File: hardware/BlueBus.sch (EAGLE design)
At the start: 128 parts, among them Q1 NMOSFET-BSS138K, Q2 PMOSFET-DMP1045UQ, Q3 NMOSFET-BSS138K, X1 CRYSTAL-12MHZ

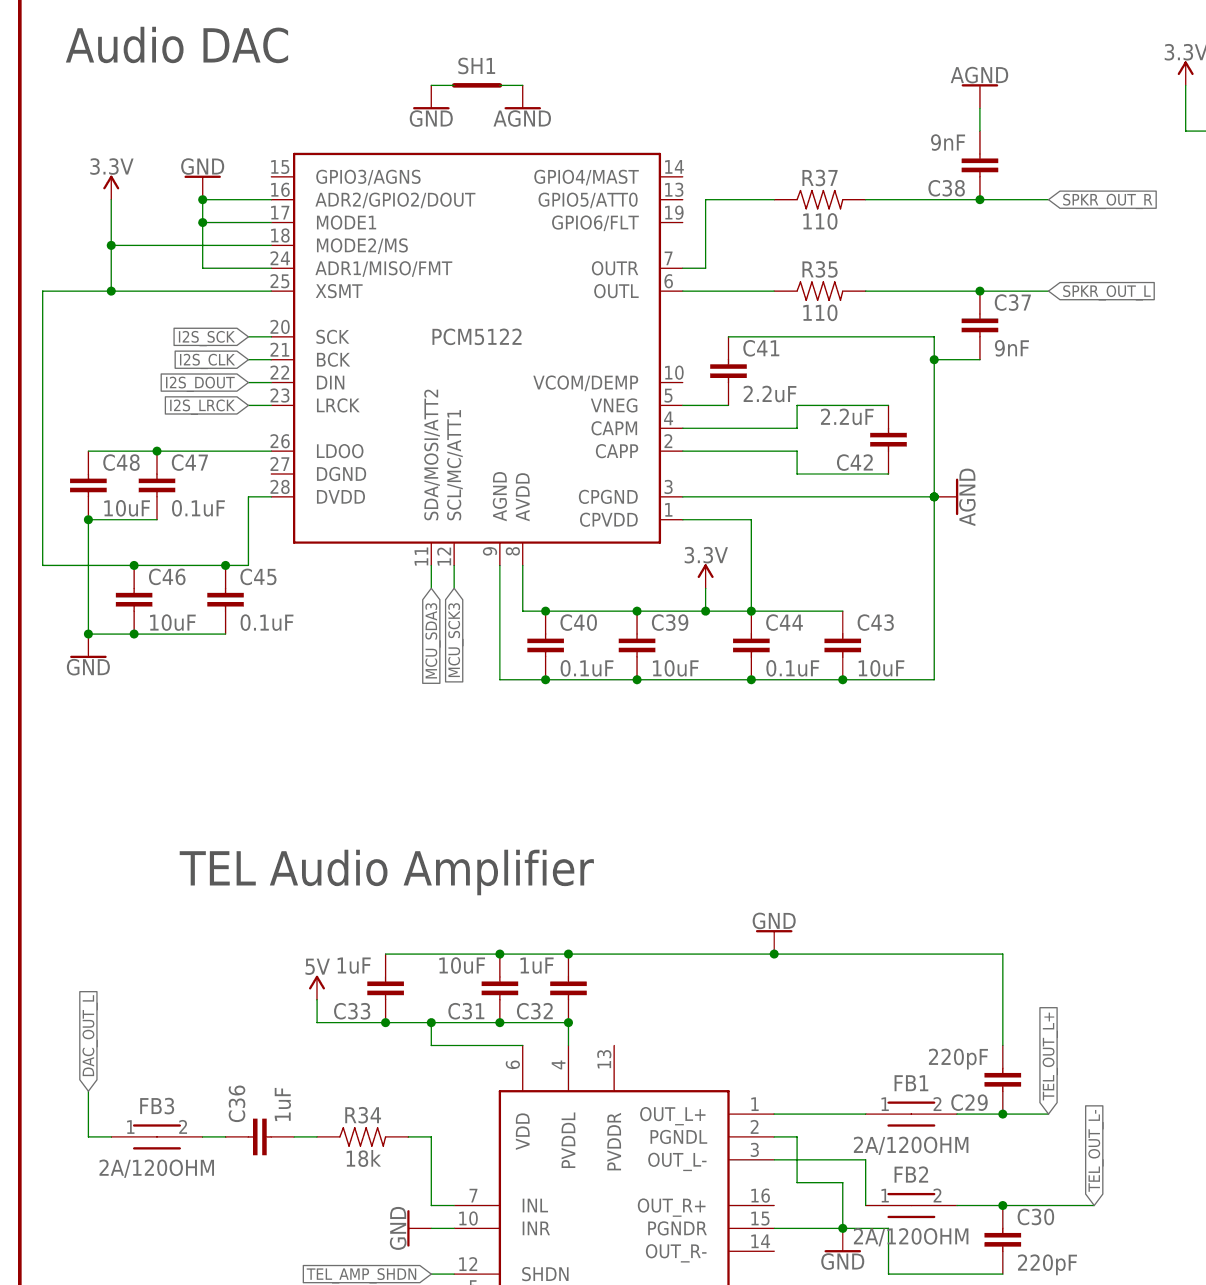
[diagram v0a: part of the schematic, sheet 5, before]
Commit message: [IMP] hardware: Revision D.1 * Remove errant layers
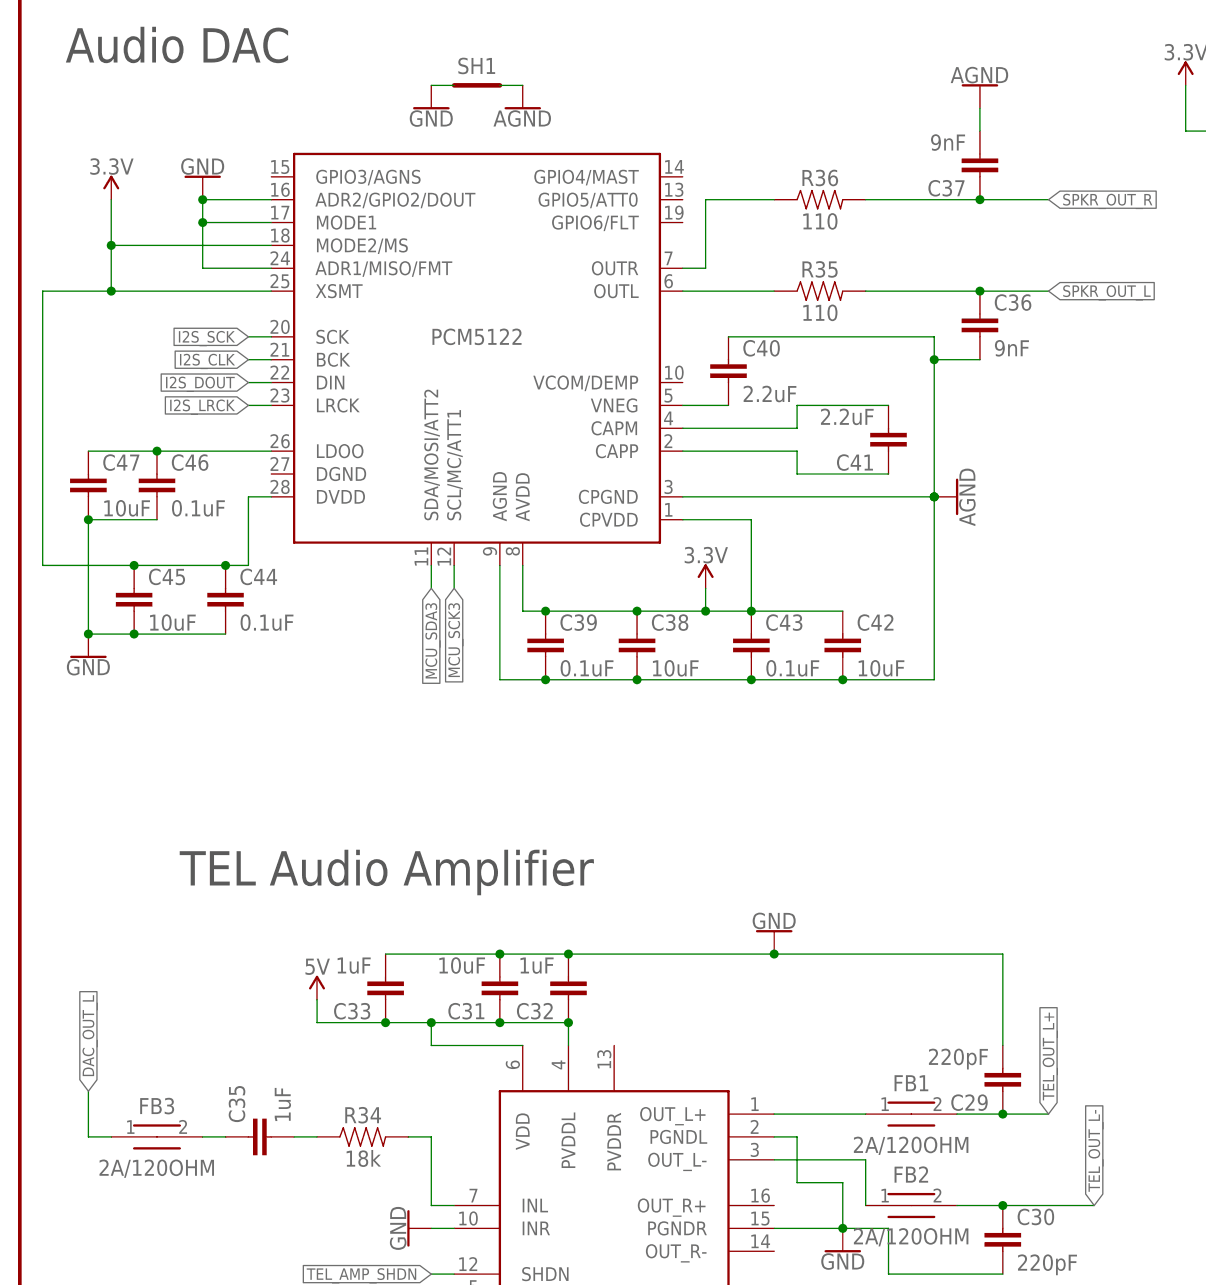
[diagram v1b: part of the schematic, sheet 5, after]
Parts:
- removed C48: 10uF, Passives:10UF2012
- added C35: 1uF, Passives:1UF
- C36: value 1uF -> 9nF; device Passives:1UF -> Passives:9NF
- C38: value 9nF -> 10uF; device Passives:9NF -> Passives:10UF2012
- C39, C43, C46: value 10uF -> 0.1uF; device Passives:10UF2012 -> Passives:0.1UF
- C40: value 0.1uF -> 2.2uF; device Passives:0.1UF -> Passives:2.2UF
- C42: value 2.2uF -> 10uF; device Passives:2.2UF -> Passives:10UF2012
- C45, C47: value 0.1uF -> 10uF; device Passives:0.1UF -> Passives:10UF2012
- renumbered R37 to R36
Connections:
- net 3.3V: now also C38.1, C42.1; no longer C40.1, C46.1
- net AGND: now also C36.2, C40.1, C42.2; no longer C40.2, C41.1, C44.2
- net DAC_CAPM: now also C41.2; no longer C42.2
- net DAC_CAPP: now also C41.1; no longer C42.1
- net DAC_LDOO: now also C46.1; no longer C48.1
- net DAC_VNEG: now also C40.2; no longer C41.2
- net GND: now also C44.2; no longer C48.2
- net SPKR_OUT_L: now also C36.1; no longer C37.1
- net SPKR_OUT_R: now also C37.1; no longer C38.1
- net TEL_AMP_IN: now also C35.1; no longer C36.1
- net TEL_AMP_INL_CAP_RES: now also C35.2; no longer C36.2
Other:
- moved on the sheet: C36, C37, C38, C39, C40, C41, C42, C43, C44, C45, C46, C47

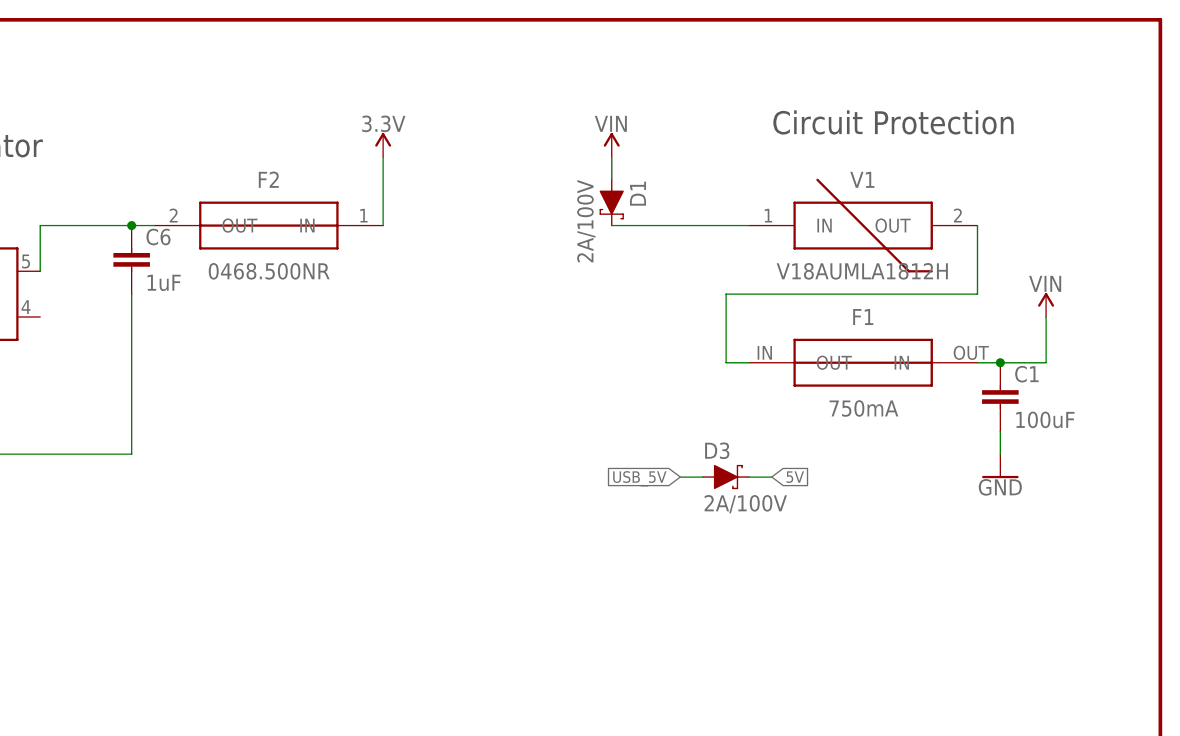
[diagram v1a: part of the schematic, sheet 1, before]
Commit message: [IMP] hardware: Update Varistor wiring * Improve Schematic drawing for circuit protection
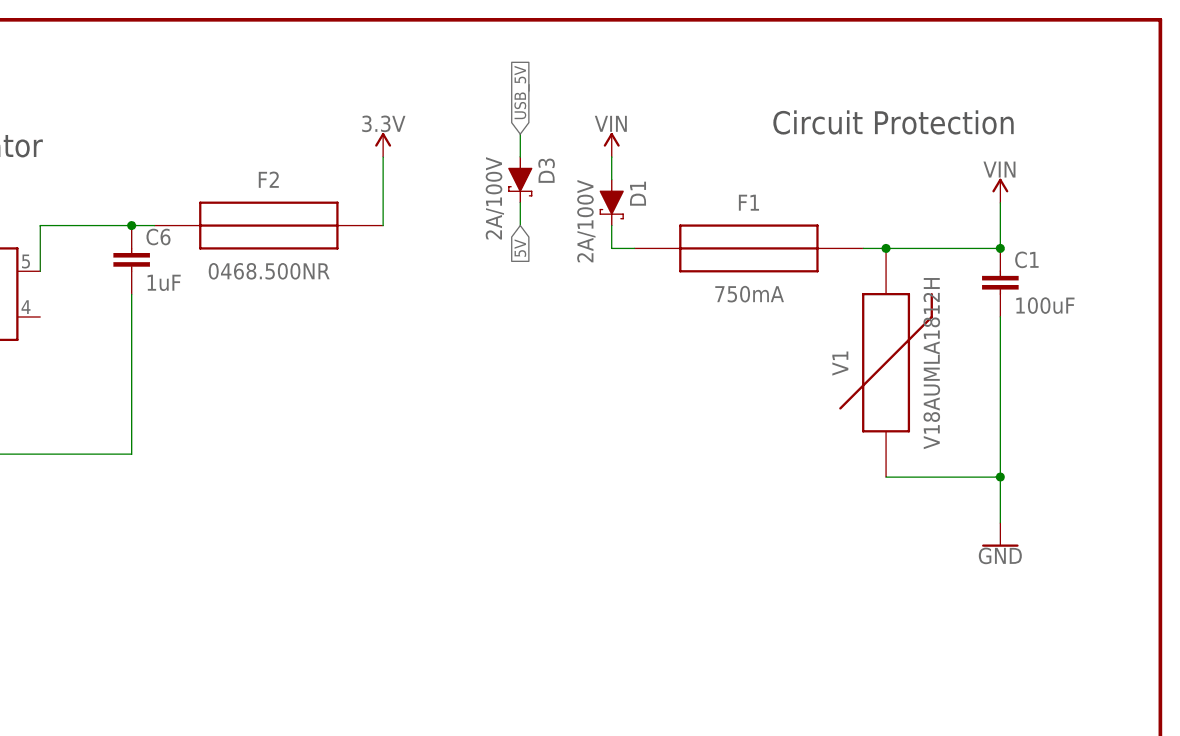
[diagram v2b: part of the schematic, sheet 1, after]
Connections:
- net GND: now also V1.IN
- net VIN: no longer V1.IN
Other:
- moved on the sheet: C1, D3
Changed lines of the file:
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@@
 <layers>
 <layer number="1" name="Top" color="4" fill="1" visible="no" active="no"/>
+<layer number="2" name="Route2" color="1" fill="3" visible="no" active="no"/>
+<layer number="3" name="Route3" color="4" fill="3" visible="no" active="no"/>
+<layer number="4" name="Route4" color="1" fill="4" visible="no" active="no"/>
+<layer number="5" name="Route5" color="4" fill="4" visible="no" active="no"/>
+<layer number="6" name="Route6" color="1" fill="8" visible="no" active="no"/>
+<layer number="7" name="Route7" color="4" fill="8" visible="no" active="no"/>
+<layer number="8" name="Route8" color="1" fill="2" visible="no" active="no"/>
+<layer number="9" name="Route9" color="4" fill="2" visible="no" active="no"/>
+<layer number="10" name="Route10" color="1" fill="7" visible="no" active="no"/>
+<layer number="11" name="Route11" color="4" fill="7" visible="no" active="no"/>
+<layer number="12" name="Route12" color="1" fill="5" visible="no" active="no"/>
+<layer number="13" name="Route13" color="4" fill="5" visible="no" active="no"/>
+<layer number="14" name="Route14" color="1" fill="6" visible="no" active="no"/>
+<layer number="15" name="Route15" color="4" fill="6" visible="no" active="no"/>
 <layer number="16" name="Bottom" color="1" fill="1" visible="no" active="no"/>
 <layer number="17" name="Pads" color="2" fill="1" visible="no" active="no"/>
@@
 <attribute name="NAME" x="71.628" y="101.6" size="1.778" layer="95" font="vector" rot="R270"/>
 </instance>
-<instance part="D3" gate="G$1" x="200.66" y="134.62" smashed="yes">
-<attribute name="NAME" x="198.12" y="136.652" size="1.778" layer="95" font="vector"/>
-<attribute name="VALUE" x="198.12" y="132.588" size="1.778" layer="96" font="vector" align="top-left"/>
-</instance>
-<instance part="C1" gate="G$1" x="231.14" y="142.24" smashed="yes">
-<attribute name="NAME" x="232.664" y="145.161" size="1.778" layer="95" font="vector"/>
-<attribute name="VALUE" x="232.664" y="140.081" size="1.778" layer="96" font="vector"/>
+<instance part="D3" gate="G$1" x="177.8" y="167.64" smashed="yes" rot="R270">
+<attribute name="NAME" x="179.832" y="170.18" size="1.778" layer="95" font="vector" rot="R270"/>
+<attribute name="VALUE" x="175.768" y="170.18" size="1.778" layer="96" font="vector" rot="R270" align="top-left"/>
+</instance>
+<instance part="C1" gate="G$1" x="231.14" y="154.94" smashed="yes">
+<attribute name="NAME" x="232.664" y="157.861" size="1.778" layer="95" font="vector"/>
+<attribute name="VALUE" x="232.664" y="152.781" size="1.778" layer="96" font="vector"/>
 </instance>
 <instance part="SPKR_OUT" gate="G$1" x="66.04" y="53.34" smashed="yes">
@@
 <attribute name="NAME" x="46.228" y="101.6" size="1.778" layer="95" font="vector" rot="R270"/>
 </instance>
-<instance part="GND17" gate="1" x="231.14" y="134.62" smashed="yes">
-<attribute name="VALUE" x="231.14" y="134.366" size="1.778" layer="96" align="top-center"/>
+<instance part="GND17" gate="1" x="231.14" y="127" smashed="yes">
+<attribute name="VALUE" x="231.14" y="126.746" size="1.778" layer="96" align="top-center"/>
 </instance>
 <instance part="XRP7659" gate="G$1" x="30.48" y="154.94" smashed="yes">
@@
 <attribute name="VALUE" x="25.4" y="14.986" size="1.778" layer="96" align="top-center"/>
 </instance>
-<instance part="V1" gate="G$1" x="215.9" y="162.56" smashed="yes">
-<attribute name="NAME" x="215.9" y="167.64" size="1.778" layer="95" font="vector" rot="MR0" align="center"/>
-<attribute name="VALUE" x="215.9" y="157.48" size="1.778" layer="96" font="vector" rot="MR0" align="center"/>
-</instance>
-<instance part="SUPPLY12" gate="G$1" x="236.22" y="152.4" smashed="yes">
-<attribute name="VALUE" x="236.22" y="155.194" size="1.778" layer="96" align="bottom-center"/>
-</instance>
-<instance part="F1" gate="G$1" x="215.9" y="147.32" smashed="yes">
-<attribute name="NAME" x="215.9" y="152.4" size="1.778" layer="95" font="vector" align="center"/>
-<attribute name="VALUE" x="215.9" y="142.24" size="1.778" layer="96" font="vector" align="center"/>
+<instance part="V1" gate="G$1" x="218.44" y="147.32" smashed="yes" rot="R90">
+<attribute name="NAME" x="213.36" y="147.32" size="1.778" layer="95" font="vector" rot="MR270" align="center"/>
+<attribute name="VALUE" x="223.52" y="147.32" size="1.778" layer="96" font="vector" rot="MR270" align="center"/>
+</instance>
+<instance part="SUPPLY12" gate="G$1" x="231.14" y="165.1" smashed="yes">
+<attribute name="VALUE" x="231.14" y="167.894" size="1.778" layer="96" align="bottom-center"/>
+</instance>
+<instance part="F1" gate="G$1" x="203.2" y="160.02" smashed="yes">
+<attribute name="NAME" x="203.2" y="165.1" size="1.778" layer="95" font="vector" align="center"/>
+<attribute name="VALUE" x="203.2" y="154.94" size="1.778" layer="96" font="vector" align="center"/>
 </instance>
 <instance part="F2" gate="G$1" x="149.86" y="162.56" smashed="yes">
@@
 <pinref part="C1" gate="G$1" pin="2"/>
 <pinref part="GND17" gate="1" pin="GND"/>
-<wire x1="231.14" y1="139.7" x2="231.14" y2="137.16" width="0.1524" layer="91"/>
+<wire x1="231.14" y1="152.4" x2="231.14" y2="134.62" width="0.1524" layer="91"/>
+<pinref part="V1" gate="G$1" pin="IN"/>
+<wire x1="231.14" y1="134.62" x2="231.14" y2="129.54" width="0.1524" layer="91"/>
+<wire x1="218.44" y1="134.62" x2="231.14" y2="134.62" width="0.1524" layer="91"/>
+<junction x="231.14" y="134.62"/>
 </segment>
 </net>
@@
 <segment>
 <pinref part="C1" gate="G$1" pin="1"/>
-<wire x1="231.14" y1="147.32" x2="236.22" y2="147.32" width="0.1524" layer="91"/>
-<wire x1="236.22" y1="147.32" x2="236.22" y2="152.4" width="0.1524" layer="91"/>
+<wire x1="231.14" y1="160.02" x2="231.14" y2="165.1" width="0.1524" layer="91"/>
 <pinref part="SUPPLY12" gate="G$1" pin="VIN"/>
-<wire x1="228.6" y1="147.32" x2="231.14" y2="147.32" width="0.1524" layer="91"/>
-<junction x="231.14" y="147.32"/>
 <pinref part="F1" gate="G$1" pin="IN"/>
+<pinref part="V1" gate="G$1" pin="OUT"/>
+<wire x1="215.9" y1="160.02" x2="218.44" y2="160.02" width="0.1524" layer="91"/>
+<wire x1="218.44" y1="160.02" x2="231.14" y2="160.02" width="0.1524" layer="91"/>
+<junction x="218.44" y="160.02"/>
+<junction x="231.14" y="160.02"/>
 </segment>
 <segment>
 <pinref part="D1" gate="G$1" pin="C"/>
-<pinref part="V1" gate="G$1" pin="IN"/>
-<wire x1="187.96" y1="162.56" x2="203.2" y2="162.56" width="0.1524" layer="91"/>
-</segment>
-<segment>
-<pinref part="V1" gate="G$1" pin="OUT"/>
-<wire x1="228.6" y1="162.56" x2="228.6" y2="154.94" width="0.1524" layer="91"/>
-<wire x1="228.6" y1="154.94" x2="200.66" y2="154.94" width="0.1524" layer="91"/>
-<wire x1="200.66" y1="154.94" x2="200.66" y2="147.32" width="0.1524" layer="91"/>
-<wire x1="200.66" y1="147.32" x2="203.2" y2="147.32" width="0.1524" layer="91"/>
+<wire x1="187.96" y1="162.56" x2="187.96" y2="160.02" width="0.1524" layer="91"/>
 <pinref part="F1" gate="G$1" pin="OUT"/>
+<wire x1="187.96" y1="160.02" x2="190.5" y2="160.02" width="0.1524" layer="91"/>
 </segment>
 </net>
@@
 <segment>
 <pinref part="D3" gate="G$1" pin="C"/>
-<wire x1="203.2" y1="134.62" x2="205.74" y2="134.62" width="0.1524" layer="91"/>
-<label x="205.74" y="134.62" size="1.27" layer="95" xref="yes"/>
+<wire x1="177.8" y1="165.1" x2="177.8" y2="162.56" width="0.1524" layer="91"/>
+<label x="177.8" y="162.56" size="1.27" layer="95" rot="R270" xref="yes"/>
 </segment>
 <segment>
@@
 <segment>
 <pinref part="D3" gate="G$1" pin="A"/>
-<wire x1="198.12" y1="134.62" x2="195.58" y2="134.62" width="0.1524" layer="91"/>
-<label x="195.58" y="134.62" size="1.27" layer="95" rot="R180" xref="yes"/>
-</segment>
-</net>
+<wire x1="177.8" y1="170.18" x2="177.8" y2="172.72" width="0.1524" layer="91"/>
+<label x="177.8" y="172.72" size="1.27" layer="95" rot="R90" xref="yes"/>
+</segment>
+</net>
